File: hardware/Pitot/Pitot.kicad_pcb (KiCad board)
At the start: 2 copper layers, 47 parts, among them IC1 ABPMRRV060MG2A3, IC2 ABPMRRV060MG2A3, J1 53307-2471, J2 Conn_01x05, J3 MX150_02x06_Vertical, U2 LDO40LPURY

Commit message: finished layout
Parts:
- removed J2: Conn_01x05, Connector_PinSocket_2.54mm:PinSocket_1x05_P2.54mm_Vertical
- added D8: LED, LED_SMD:LED_0603_1608Metric_Pad1.05x0.95mm_HandSolder, F.Cu at (93.4, 38.6)
- added D9: LED, LED_SMD:LED_0603_1608Metric_Pad1.05x0.95mm_HandSolder, F.Cu at (93.4, 37.1)
- added G***: LHRs_LOGO, UTSVT_Logos:LHRs_LOGO, F.Cu at (96.9, 80.8)
- added J4: Conn_01x07, Connector_PinHeader_2.54mm:PinHeader_2x04_P2.54mm_Vertical, B.Cu at (72.3, 58.2)
- added R18: 4.7k, Resistor_SMD:R_0603_1608Metric_Pad0.98x0.95mm_HandSolder, F.Cu at (59.6, 56.7)
- added R19: 4.7k, Resistor_SMD:R_0603_1608Metric_Pad0.98x0.95mm_HandSolder, F.Cu at (60.0, 82.8)
- +3.3MCU1, GND2, J3, PressERR1, PressERR2: moved to B.Cu
- R12, R14, R16, R17, R7, R8: value 1k -> 120
- R13, R15: value 0 -> 120
- moved R11 80.5 mm to (65.0, 36.2)
- moved R10 79.6 mm to (65.0, 34.6)
- moved IC1 68.8 mm to (61.6, 44.1), turned to 180 degrees
- moved R9 66.7 mm to (58.7, 53.9), turned to -90 degrees
- moved C5 66.3 mm to (61.4, 54.6)
- moved C6 63.7 mm to (61.4, 52.9)
- moved PressERR1 57.9 mm to (65.5, 57.5), turned to 180 degrees
- moved PressERR2 56.5 mm to (68.7, 80.2), turned to 180 degrees
- moved F1 52.5 mm to (84.5, 37.7), turned to 180 degrees
- moved R6 49.5 mm to (59.9, 62.0)
- moved R5 48.6 mm to (59.9, 60.5)
- moved RN1 47.3 mm to (82.3, 73.3), turned to 90 degrees
- moved U2 45.0 mm to (96.9, 49.6), turned to 180 degrees
- moved RN2 36.8 mm to (88.2, 73.3), turned to -90 degrees
- moved IC2 36.2 mm to (61.3, 70.1), turned to 180 degrees
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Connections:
- net /CAN_H renamed /CAN_+
- net /CAN_L renamed /CAN_-
- C1 pad 1: +3.3V -> Net-(U2-Vout)
- C3 pad 1: +3.3VMCU -> +3.3V
- C4 pad 1: +3.3VMCU -> +3.3V
- C5 pad 1: +3.3VMCU -> +3.3V
- C6 pad 1: +3.3VMCU -> +3.3V
- D4 pad 1: Net-(D4-K) -> GND
- D5 pad 1: Net-(D5-K) -> GND
- IC1 pad 2: +3.3VMCU -> +3.3V
- IC2 pad 2: +3.3VMCU -> +3.3V
- J1 pad 12: unconnected-(J1-SPI2_NSS-Pad12) -> /P2_LED
- J1 pad 15: unconnected-(J1-ADC1_IN11-Pad15) -> /P1_LED
- J1 pad 16: unconnected-(J1-SPI2_MOSI-Pad16) -> /Debug1
- J1 pad 19: unconnected-(J1-SPI1_NSS-Pad19) -> /Debug2
- R12 pad 1: +3.3V -> /P1_LED
- R13 pad 1: Net-(D4-K) -> /Debug2
- R13 pad 2: GND -> Net-(D8-A)
- R14 pad 1: +3.3V -> /P2_LED
- R15 pad 1: Net-(D5-K) -> /Debug1
- R15 pad 2: GND -> Net-(D9-A)
- RN1 pad 2: /Gen_2 -> /Gen_3
- RN1 pad 3: /Gen_3 -> /Gen_2
- RN1 pad 6: /SDA2 -> /SCL2
- RN1 pad 7: /SCL2 -> /SDA2
- RN2 pad 1: /Gen_1 -> /Gen_4
- RN2 pad 4: /Gen_4 -> /Gen_1
- RN2 pad 5: GND -> +24V
- RN2 pad 8: +24V -> GND
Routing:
- net +24V: track 0.00 -> 91.8 mm, vias 0 -> 4
- net /pressERR_2: track 0.00 -> 79.2 mm, vias 0 -> 5
- net /SCL1: track 0.00 -> 78.7 mm, vias 0 -> 4
- net /SDA1: track 0.00 -> 77.7 mm, vias 0 -> 3
- net /SDA2: track 0.00 -> 73.0 mm, vias 0 -> 4
- net /pressERR_1: track 0.00 -> 72.5 mm, vias 0 -> 7
- net /SCL2: track 0.00 -> 58.4 mm, vias 0 -> 2
- net GND: track 0.00 -> 48.5 mm, vias 0 -> 17
- net +3.3V: track 0.00 -> 45.1 mm, vias 0 -> 14
- net /P1_LED: track 0.00 -> 44.2 mm, vias 0 -> 4
- net /CAN_-: track 0.00 -> 41.4 mm
- net /CAN_+: track 0.00 -> 40.7 mm
- net Net-(U2-Vout): track 0.00 -> 25.5 mm
- net /Gen_1: track 0.00 -> 23.0 mm, vias 0 -> 1
- net /Gen_3: track 0.00 -> 20.3 mm
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- added copper zone on F.Cu, net +3.3V
- added copper zone on B.Cu, net GND
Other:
- board outline added: 51.7 x 61.1 mm
- board text added: "+24v"
- board text added: "+3.3v"
- board text added: "Config"
- board text added: "Debug"
- board text added: "Karthik Kurapati"
- board text added: "MCU"
- board text added: "P1"
- board text added: "P2"
- board text added: "Power"
- board text added: "Pressure"
- board text added: "Status"
- board text added: "Temperature"

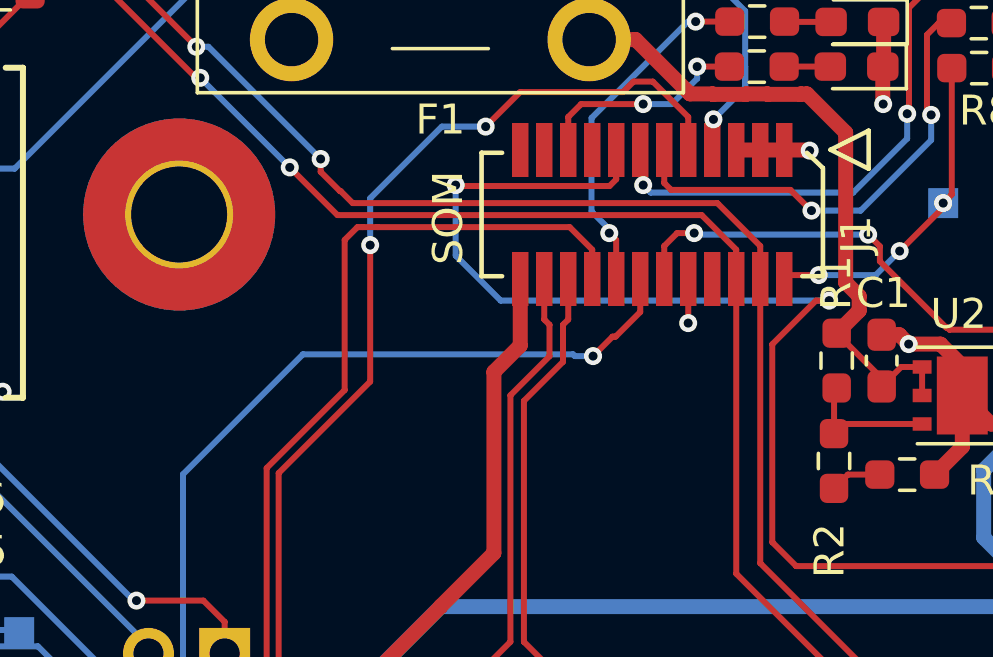
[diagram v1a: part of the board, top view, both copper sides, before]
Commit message: added silkscreen, fixed rh-sus layout rh-sus done
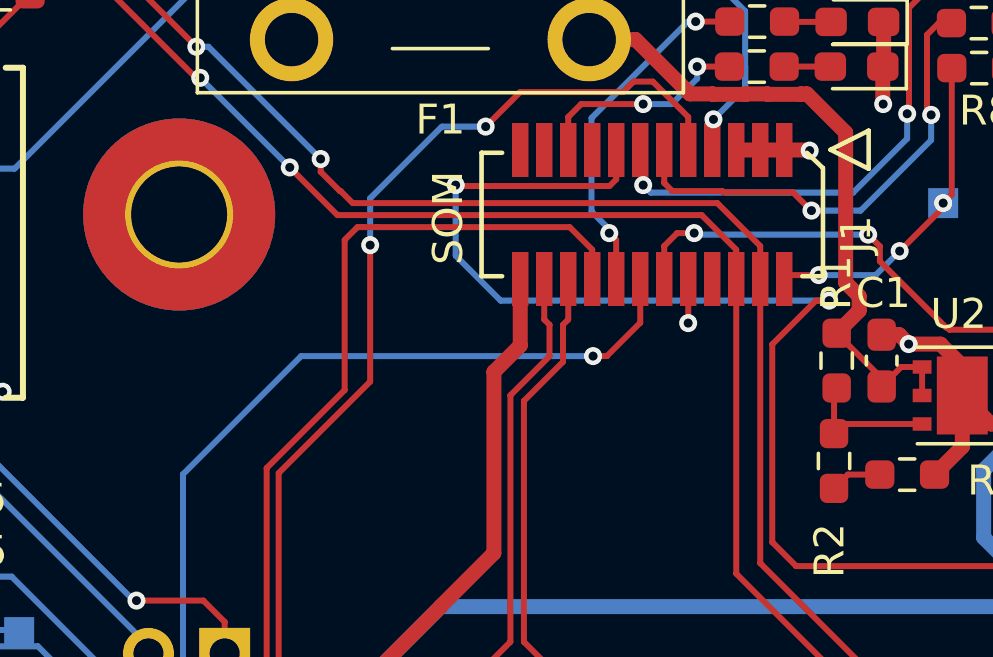
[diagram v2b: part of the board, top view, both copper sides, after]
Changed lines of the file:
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@@
-	)
-	(segment
-		(start 86.2025 46.78)
-		(end 86.2025 45.68)
-		(width 0.2)
-		(layer "F.Cu")
-		(net 19)
 	)
 	(segment
@@
 	)
 	(segment
+		(start 86.2025 45.68)
+		(end 86.2025 47.1375)
+		(width 0.2)
+		(layer "F.Cu")
+		(net 19)
+	)
+	(segment
 		(start 67.8 68.1)
 		(end 73.9 68.1)
@@
 	)
 	(segment
+		(start 85.09 48.25)
+		(end 84.63 48.25)
+		(width 0.2)
+		(layer "F.Cu")
+		(net 19)
+	)
+	(segment
 		(start 73.9 68.1)
 		(end 73.95 68.05)
@@
 	)
 	(segment
+		(start 86.2025 47.1375)
+		(end 85.09 48.25)
+		(width 0.2)
+		(layer "F.Cu")
+		(net 19)
+	)
+	(segment
 		(start 60.0365 61.2885)
 		(end 60.825 60.5)
@@
 		(net 19)
 	)
+	(via
+		(at 84.63 48.25)
+		(size 0.6)
+		(drill 0.3)
+		(layers "F.Cu" "B.Cu")
+		(net 19)
+	)
+	(via
+		(at 67.8 68.1)
+		(size 0.6)
+		(drill 0.3)
+		(layers "F.Cu" "B.Cu")
+		(net 19)
+	)
+	(via
+		(at 62.275 65.775)
+		(size 0.6)
+		(drill 0.3)
+		(layers "F.Cu" "B.Cu")
+		(net 19)
+	)
+	(via
+		(at 62 60.5)
+		(size 0.6)
+		(drill 0.3)
+		(layers "F.Cu" "B.Cu")
+		(net 19)
+	)
+	(segment
+		(start 62 60.5)
+		(end 61.149 59.649)
+		(width 0.2)
+		(layer "B.Cu")
+		(net 19)
+	)
 	(segment
 		(start 84.63 48.25)
-		(end 85.28 47.6)
-		(width 0.2)
-		(layer "F.Cu")
-		(net 19)
-	)
-	(segment
-		(start 85.28 47.6)
-		(end 85.3825 47.6)
-		(width 0.2)
-		(layer "F.Cu")
-		(net 19)
-	)
-	(segment
-		(start 85.3825 47.6)
-		(end 86.2025 46.78)
-		(width 0.2)
-		(layer "F.Cu")
-		(net 19)
-	)
-	(via
-		(at 84.63 48.25)
-		(size 0.6)
-		(drill 0.3)
-		(layers "F.Cu" "B.Cu")
-		(net 19)
-	)
-	(via
-		(at 67.8 68.1)
-		(size 0.6)
-		(drill 0.3)
-		(layers "F.Cu" "B.Cu")
-		(net 19)
-	)
-	(via
-		(at 62.275 65.775)
-		(size 0.6)
-		(drill 0.3)
-		(layers "F.Cu" "B.Cu")
-		(net 19)
-	)
-	(via
-		(at 62 60.5)
-		(size 0.6)
-		(drill 0.3)
-		(layers "F.Cu" "B.Cu")
+		(end 74.9 48.25)
+		(width 0.2)
+		(layer "B.Cu")
 		(net 19)
 	)
@@
 	)
 	(segment
-		(start 62 60.5)
-		(end 61.149 59.649)
-		(width 0.2)
-		(layer "B.Cu")
-		(net 19)
-	)
-	(segment
-		(start 84.02 48.25)
-		(end 83.96 48.19)
-		(width 0.2)
-		(layer "B.Cu")
-		(net 19)
-	)
-	(segment
-		(start 83.96 48.19)
-		(end 74.96 48.19)
+		(start 65.252 55.6)
+		(end 69.81 60.158)
+		(width 0.2)
+		(layer "B.Cu")
+		(net 19)
+	)
+	(segment
+		(start 74.9 48.25)
+		(end 70.961 52.189)
+		(width 0.2)
+		(layer "B.Cu")
+		(net 19)
+	)
+	(segment
+		(start 62.000057 55.6)
+		(end 65.252 55.6)
+		(width 0.2)
+		(layer "B.Cu")
+		(net 19)
+	)
+	(segment
+		(start 67.75 68.05)
+		(end 67.8 68.1)
+		(width 0.2)
+		(layer "B.Cu")
+		(net 19)
+	)
+	(segment
+		(start 69.81 60.158)
+		(end 69.81 60.7)
+		(width 0.2)
+		(layer "B.Cu")
+		(net 19)
+	)
+	(segment
+		(start 64.55 68.05)
+		(end 67.75 68.05)
+		(width 0.2)
+		(layer "B.Cu")
+		(net 19)
+	)
+	(segment
+		(start 61.149 59.649)
+		(end 61.149 56.451057)
+		(width 0.2)
+		(layer "B.Cu")
+		(net 19)
+	)
+	(segment
+		(start 62.275 65.775)
+		(end 64.55 68.05)
 		(width 0.2)
 		(layer "B.Cu")
@@
 	)
 	(segment
-		(start 65.252 55.6)
-		(end 69.81 60.158)
-		(width 0.2)
-		(layer "B.Cu")
-		(net 19)
-	)
-	(segment
-		(start 74.96 48.19)
-		(end 70.961 52.189)
-		(width 0.2)
-		(layer "B.Cu")
-		(net 19)
-	)
-	(segment
-		(start 62.000057 55.6)
-		(end 65.252 55.6)
-		(width 0.2)
-		(layer "B.Cu")
-		(net 19)
-	)
-	(segment
-		(start 67.75 68.05)
-		(end 67.8 68.1)
-		(width 0.2)
-		(layer "B.Cu")
-		(net 19)
-	)
-	(segment
-		(start 69.81 60.158)
-		(end 69.81 60.7)
-		(width 0.2)
-		(layer "B.Cu")
-		(net 19)
-	)
-	(segment
-		(start 64.55 68.05)
-		(end 67.75 68.05)
-		(width 0.2)
-		(layer "B.Cu")
-		(net 19)
-	)
-	(segment
-		(start 61.149 59.649)
-		(end 61.149 56.451057)
-		(width 0.2)
-		(layer "B.Cu")
-		(net 19)
-	)
-	(segment
-		(start 62.275 65.775)
-		(end 64.55 68.05)
-		(width 0.2)
-		(layer "B.Cu")
-		(net 19)
-	)
-	(segment
-		(start 84.63 48.25)
-		(end 84.02 48.25)
-		(width 0.2)
-		(layer "B.Cu")
-		(net 19)
-	)
-	(segment
 		(start 61.149 56.451057)
 		(end 62.000057 55.6)
@@
 	)
 	(segment
+		(start 87.002503 42.48)
+		(end 87.002503 41.38)
+		(width 0.2)
+		(layer "F.Cu")
+		(net 26)
+	)
+	(segment
+		(start 95.76 37.54)
+		(end 96.15 37.15)
+		(width 0.2)
+		(layer "F.Cu")
+		(net 26)
+	)
+	(segment
+		(start 88.9386 42.749)
+		(end 87.271503 42.749)
+		(width 0.2)
+		(layer "F.Cu")
+		(net 26)
+	)
+	(segment
+		(start 95.9 40.15)
+		(end 95.76 40.01)
+		(width 0.2)
+		(layer "F.Cu")
+		(net 26)
+	)
+	(segment
 		(start 91.85 43.35)
-		(end 91.21 42.71)
+		(end 91.29 42.79)
 		(width 0.2)
 		(layer "F.Cu")
@@
 	)
 	(segment
-		(start 95.76 37.54)
-		(end 96.15 37.15)
-		(width 0.2)
-		(layer "F.Cu")
-		(net 26)
-	)
-	(segment
-		(start 95.9 40.15)
-		(end 95.76 40.01)
+		(start 91.29 42.79)
+		(end 88.9796 42.79)
 		(width 0.2)
 		(layer "F.Cu")
@@
 	)
 	(segment
+		(start 88.9796 42.79)
+		(end 88.9386 42.749)
+		(width 0.2)
+		(layer "F.Cu")
+		(net 26)
+	)
+	(segment
 		(start 95.76 40.01)
 		(end 95.76 37.54)
@@
 	)
 	(segment
-		(start 87.002503 42.48)
-		(end 87.002503 41.38)
-		(width 0.2)
-		(layer "F.Cu")
-		(net 26)
-	)
-	(segment
-		(start 87.232503 42.71)
+		(start 87.271503 42.749)
 		(end 87.002503 42.48)
 		(width 0.2)
 		(layer "F.Cu")
-		(net 26)
-	)
-	(segment
-		(start 91.21 42.71)
-		(end 87.232503 42.71)
-		(width 0.2)
-		(layer "F.Cu")

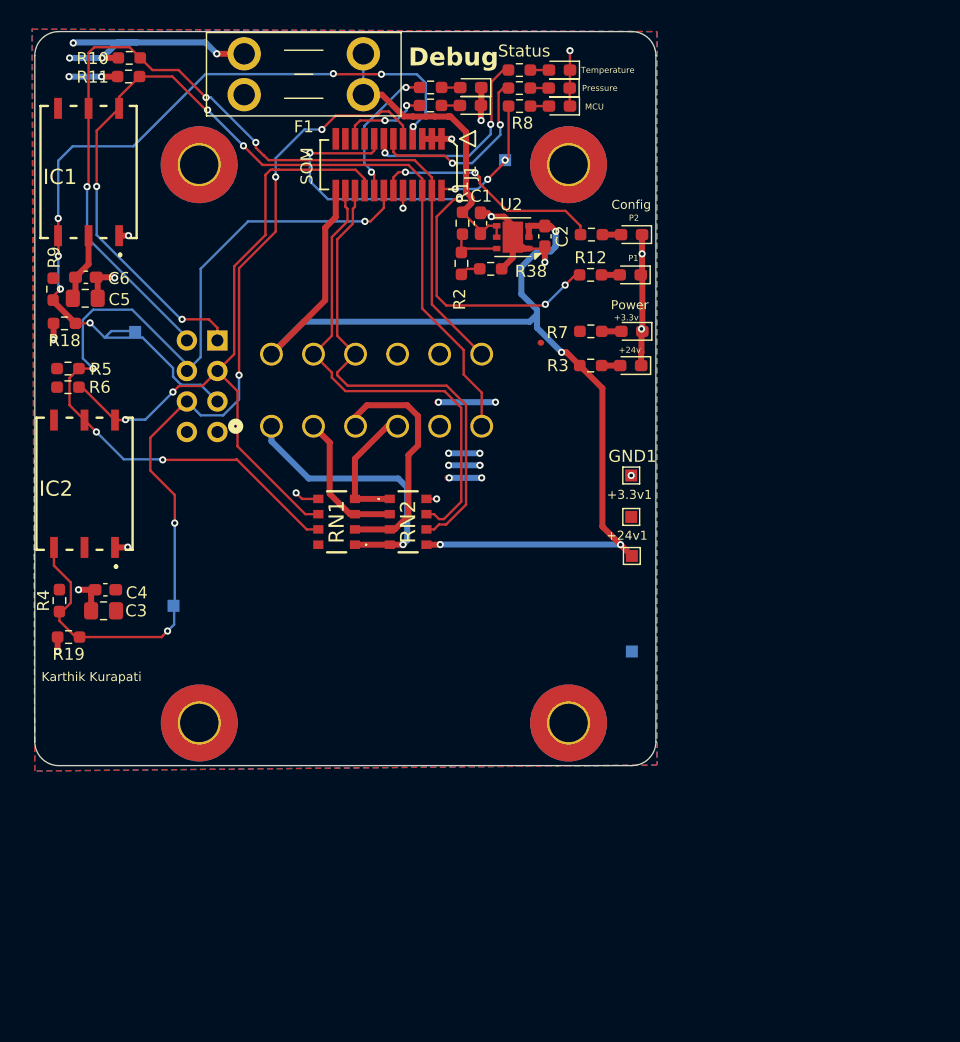
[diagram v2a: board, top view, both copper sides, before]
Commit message: fixed routing for air-sus, should be much better now. added silkscreen
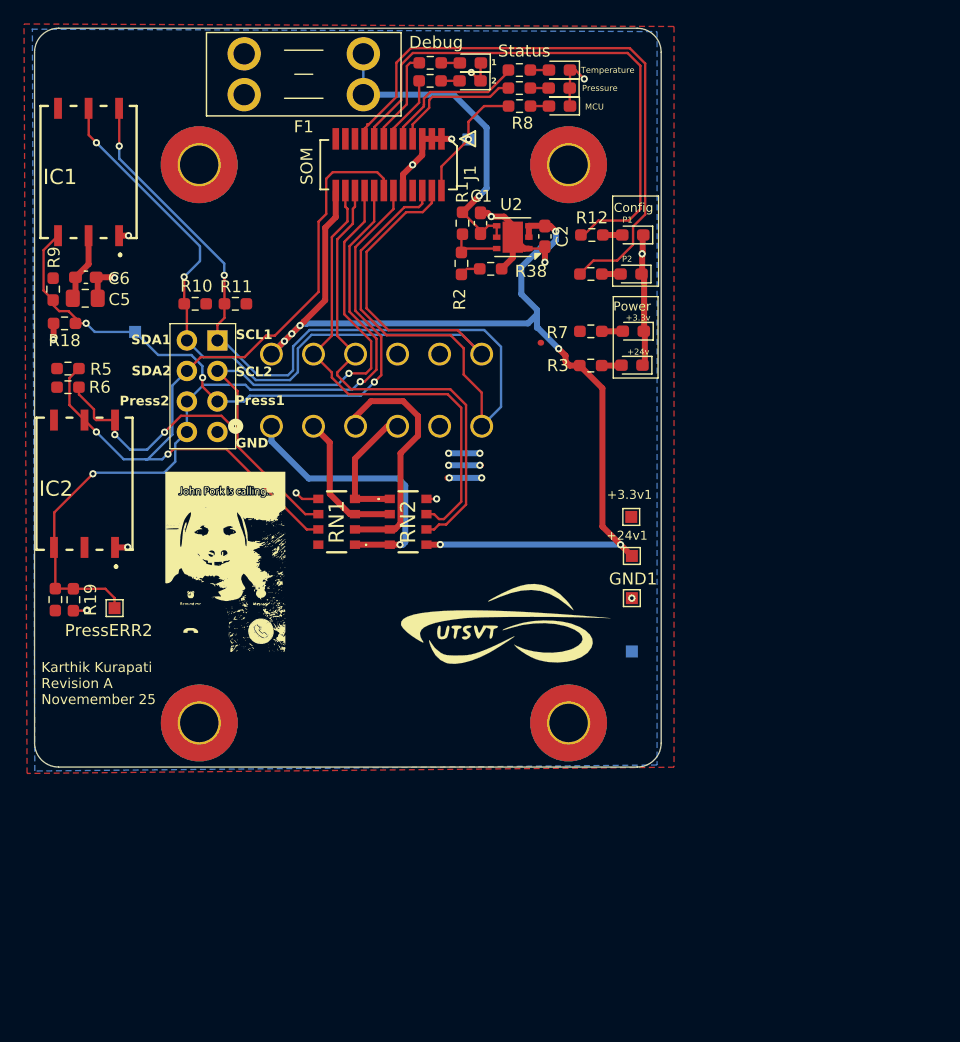
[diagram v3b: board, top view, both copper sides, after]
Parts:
- removed C3: 10uf, Capacitor_SMD:C_0805_2012Metric_Pad1.18x1.45mm_HandSolder
- removed C4: 0.1uF, Capacitor_SMD:C_0603_1608Metric_Pad1.08x0.95mm_HandSolder
- added G***: LOGO, footprints:johnInverted, F.Cu at (73.0, 76.6)
- added G***: LOGO, UTSVT_Logos:UTSVT_Logo_Symbol, F.Cu at (96.1, 81.9)
- added G***: LOGO, footprints:diddybludInverted, B.Cu at (94.8, 82.1)
- added G***: LOGO, UTSVT_Logos:roosters, B.Cu at (84.2, 48.7)
- PressERR2: moved to F.Cu
- R3: value 1k -> 4.7k
- moved G*** 55.3 mm to (65.2, 35.5)
- moved R10 21.2 mm to (70.5, 55.1), turned to 180 degrees
- moved R11 20.9 mm to (73.8, 55.1), turned to 180 degrees
- moved GND1 10.2 mm to (106.8, 79.6)
- moved PressERR2 4.91 mm to (63.8, 80.4), turned to 0 degrees
- moved +3.3MCU1 3.50 mm to (93.2, 41.4)
- moved D4 3.33 mm to (106.9, 49.4)
- moved R12 3.32 mm to (103.5, 49.4)
- moved D5 3.28 mm to (106.8, 52.6)
- moved R14 3.28 mm to (103.4, 52.6)
- moved R19 3.13 mm to (60.4, 79.7), turned to -90 degrees
- moved D8 2.05 mm to (93.4, 36.5)
- moved R13 2.05 mm to (90.1, 36.5)
- moved R15 2.05 mm to (90.1, 35.0)
- moved D9 2.05 mm to (93.4, 35.1)
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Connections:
- J1 pad 11: /diff_stat -> /Debug2
- J1 pad 12: /P2_LED -> /pressERR_1
- J1 pad 13: /temp_stat -> /Debug1
- J1 pad 16: /Debug1 -> /pressERR_2
- J1 pad 17: unconnected-(J1-SPI1_MOSI-Pad17) -> /P2_LED
- J1 pad 19: /Debug2 -> unconnected-(J1-SPI1_NSS-Pad19)
- J1 pad 7: /pressERR_1 -> /diff_stat
- J1 pad 9: /pressERR_2 -> /temp_stat
- J4 pad 8: (no net) -> /pressERR_2
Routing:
- net +3.3V: track 45.1 -> 14.0 mm, vias 14 -> 6
- net /P2_LED: track 20.1 -> 50.2 mm, vias 2 -> 0
- net /pressERR_1: track 72.5 -> 57.0 mm, vias 7 -> 3
- net /pressERR_2: track 79.2 -> 64.1 mm, vias 5 -> 2
- net /SCL1: track 78.7 -> 89.4 mm, vias 4 -> 2
- net /SCL2: track 58.4 -> 65.7 mm, vias 2 -> 3
- net /SDA2: track 73.2 -> 67.5 mm, vias 4 -> 2
- net /diff_stat: track 15.9 -> 10.8 mm, vias 2 -> 0
- net /temp_stat: track 17.1 -> 12.2 mm, vias 2 -> 0
- net /Debug1: track 11.6 -> 8.00 mm, vias 2 -> 0
- net Net-(U2-Vout): track 25.5 -> 27.7 mm, vias 0 -> 1
- net /Debug2: track 7.40 -> 5.72 mm, vias 2 -> 0
- net /P1_LED: track 44.2 -> 45.6 mm, vias 4 -> 0
- net +3.3VMCU: track 11.2 -> 10.6 mm, vias 3 -> 1
- net /SDA1: track 77.7 -> 77.1 mm, vias 3 -> 2
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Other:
- board size 51.7 x 61.1 mm -> 52.2 x 61.5 mm
- board text added: "1"
- board text added: "2"
- board text added: "GND"
- board text added: "Karthik Kurapati Revision A Novemember 25"
- board text added: "Press1"
- board text added: "Press2"
- board text added: "SCL1"
- board text added: "SCL2"
- board text added: "SDA1"
- board text added: "SDA2"
- board text removed: "Karthik Kurapati"

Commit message: small changes
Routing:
- net /SCL1: track 89.4 -> 87.2 mm
- net /SDA1: track 77.1 -> 75.3 mm
- net /pressERR_2: track 64.1 -> 63.4 mm
- net /pressERR_1: track 57.0 -> 56.3 mm
- net /SCL2: track 65.7 -> 65.1 mm
